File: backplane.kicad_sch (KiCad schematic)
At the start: 6 parts, among them J16 PCB-Edge_Samtec_HSEC8_2x20_HS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, U12 ESD204DQAR, U13 ESD204DQAR, U14 ESD204DQAR, U15 ESD204DQAR, U16 ESD204DQAR

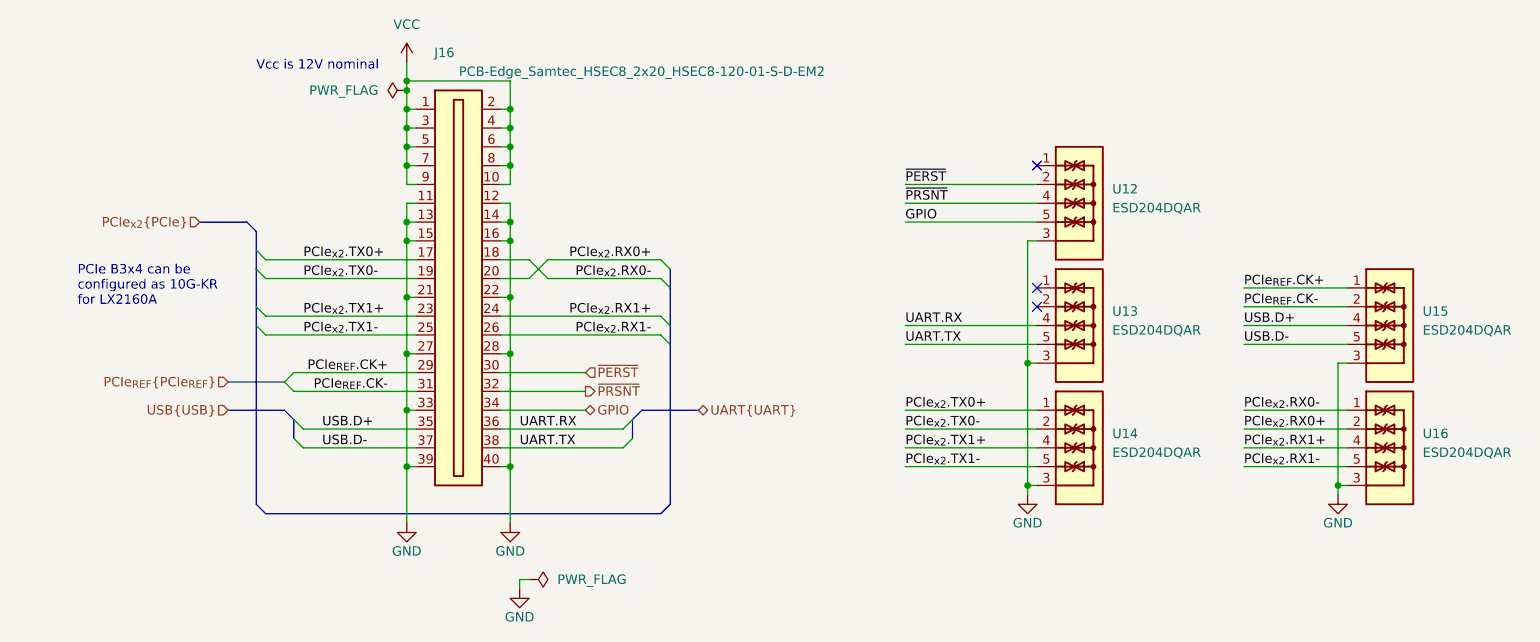
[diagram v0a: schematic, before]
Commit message: [#70030] Routed PCIe
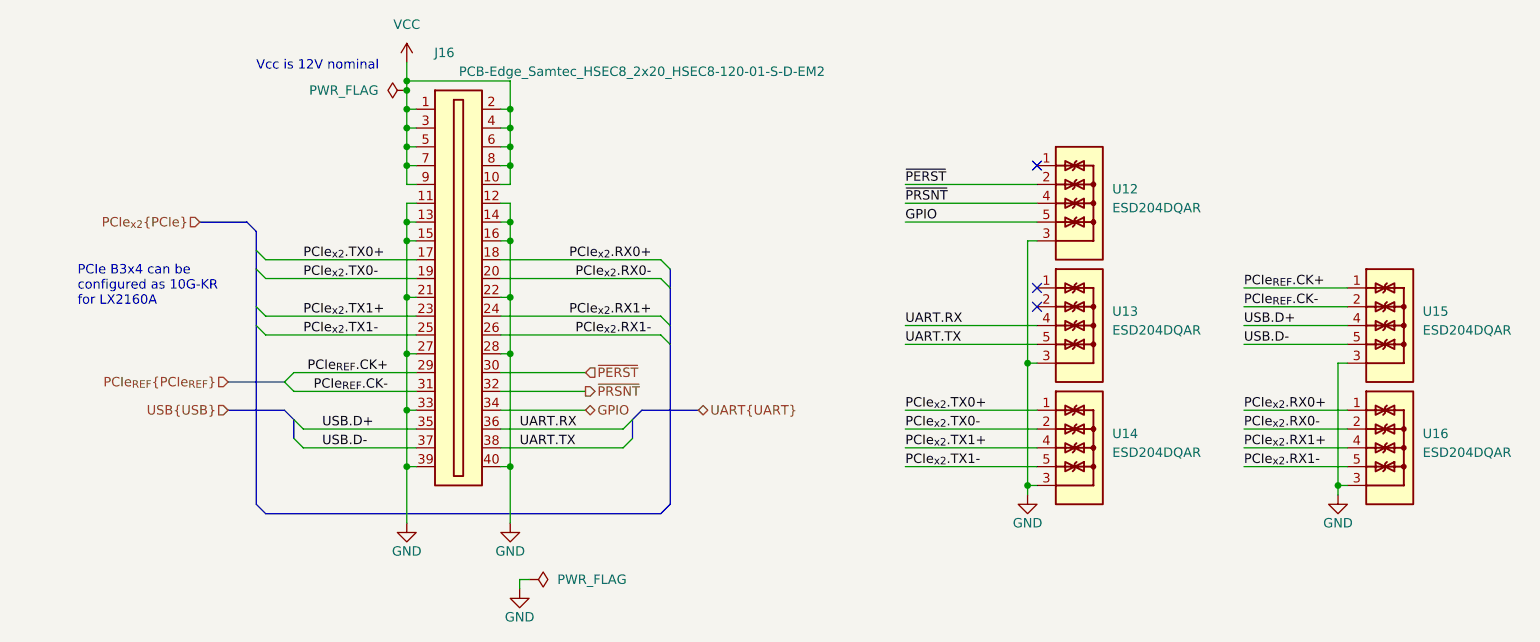
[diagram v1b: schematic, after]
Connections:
- net PCIe_{x2}.RX0+: now also J16.18, U16.1, U16.10; no longer J16.20, U16.2, U16.9
- net PCIe_{x2}.RX0-: now also J16.20, U16.2, U16.9; no longer J16.18, U16.1, U16.10
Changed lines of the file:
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@@
 	(wire
 		(pts
-			(xy 203.2 147.32) (xy 207.01 147.32)
+			(xy 203.2 147.32) (xy 224.79 147.32)
 		)
 		(stroke
@@
 	(wire
 		(pts
-			(xy 207.01 144.78) (xy 209.55 147.32)
-		)
-		(stroke
-			(width 0)
-			(type default)
-		)
-	)
-	(wire
-		(pts
 			(xy 274.32 175.26) (xy 274.32 176.53)
 		)
@@
 	(wire
 		(pts
-			(xy 203.2 144.78) (xy 207.01 144.78)
+			(xy 203.2 144.78) (xy 224.79 144.78)
 		)
 		(stroke
@@
 		)
 	)
-	(wire
-		(pts
-			(xy 209.55 144.78) (xy 207.01 147.32)
-		)
-		(stroke
-			(width 0)
-			(type default)
-		)
-	)
 	(bus
 		(pts
@@
 		)
 	)
-	(wire
-		(pts
-			(xy 209.55 147.32) (xy 224.79 147.32)
-		)
-		(stroke
-			(width 0)
-			(type default)
-		)
-	)
 	(bus
 		(pts
 			(xy 171.45 179.07) (xy 170.18 177.8)
-		)
-		(stroke
-			(width 0)
-			(type default)
-		)
-	)
-	(wire
-		(pts
-			(xy 209.55 144.78) (xy 224.79 144.78)
 		)
 		(stroke
@@
 	)
 	(label "PCIe_{x2}.RX0-"
-		(at 303.53 165.1 0)
+		(at 303.53 167.64 0)
 		(fields_autoplaced yes)
 		(effects
@@
 	)
 	(label "PCIe_{x2}.RX0+"
-		(at 303.53 167.64 0)
-		(fields_autoplaced yes)
-		(effects
+		(at 303.53 165.1 0)
+		(fields_autoplaced yes)
+		(effects
